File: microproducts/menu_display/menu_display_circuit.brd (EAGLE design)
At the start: 68.6 x 53.3 mm, 3 parts

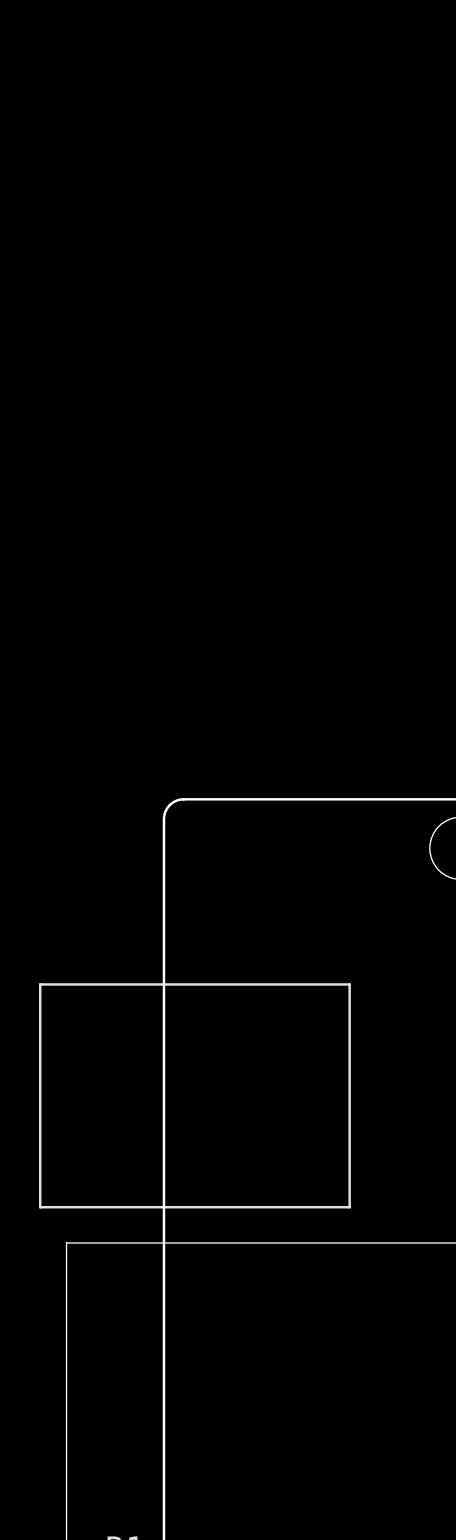
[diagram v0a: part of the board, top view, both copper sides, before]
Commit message: added 3 buttons to change displayed number
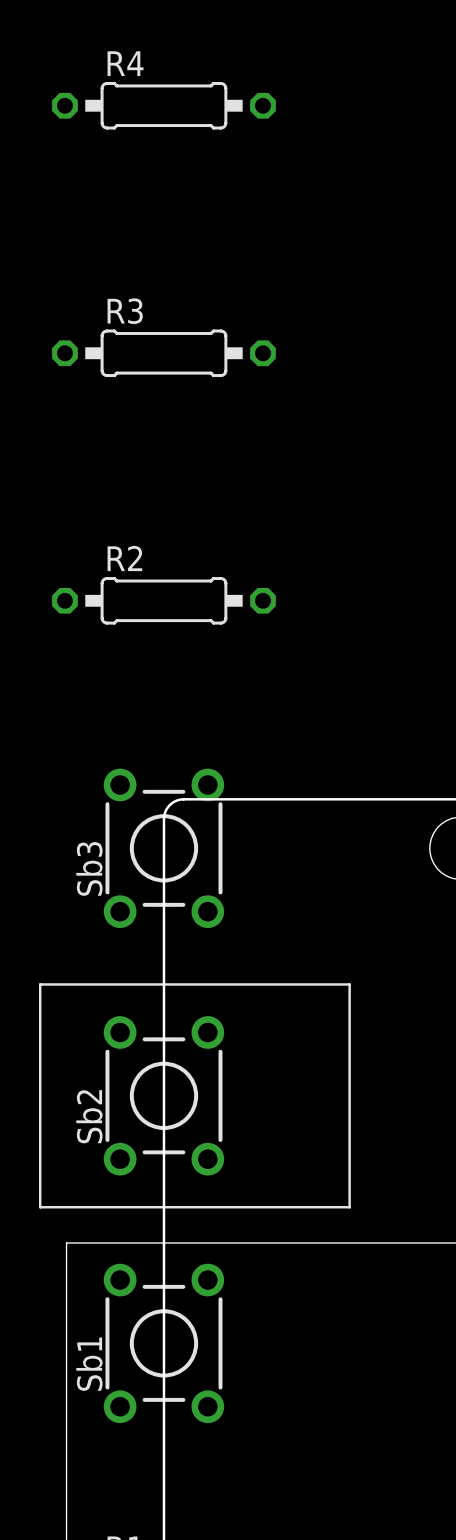
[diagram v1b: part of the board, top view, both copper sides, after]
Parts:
- added R2, R3, R4: 10k‎Ω, AUTODESK_CIRCUITS_BREADBOARD:0207/10
- added Sb1, Sb2, Sb3: (no value), AUTODESK_CIRCUITS_BREADBOARD:TL1105
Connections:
- removed net N$12 (its old number): Uarduino.GND, Ulcd.1, Ulcd.16, Ulcd.3, Ulcd.5
- removed net N$13 (its old number): R1.2, Uarduino.5V, Ulcd.2
- new net N$10: R4.1, Sb3.1, Sb3.3, Uarduino.10
- new net N$15: R1.2, Sb1.2, Sb1.4, Sb2.2, Sb2.4, Sb3.2, Sb3.4, Uarduino.5V, Ulcd.2
- new net N$16: R2.2, R3.2, R4.2, Uarduino.GND, Ulcd.1, Ulcd.16, Ulcd.3, Ulcd.5
- new net N$8: R2.1, Sb1.1, Sb1.3, Uarduino.8
- new net N$9: R3.1, Sb2.1, Sb2.3, Uarduino.9
